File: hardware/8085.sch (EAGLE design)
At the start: 59 parts, among them IC10 74HCT00N, IC11 74HCT245DW, IC2 74HCT574N, IC3 ATF16V8BP3, IC4 74AC00D, IC5 74HCT245DW, IC6 74AC273N, IC7 74HCT139N, IC9 74HCT138N

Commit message: CPU board design updated. 7474 chip added to synchronize address decoders activity with ALE line.
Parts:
- added C12: 100n, rcl:C-EUC0805
- added IC8: 74HCT74N, 74xx-eu:74HCT74N
- added R18: (no value), rcl:R-EU_0204/5
- R17: device rcl:R-EU_0207/10 -> rcl:R-EU_0204/7
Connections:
- new net IO_M_SYNC: IC3.I5, IC8B.Q, IC9A.G1
- new net N$17: IC8A.PRE, IC8B.CLR, IC8B.PRE, R18.1
- net !ALE: now also IC8B.CLK
- net GND: now also C12.2, IC8A.CLK, IC8A.CLR, IC8A.D
- net IO_M: now also IC8B.D; no longer IC3.I5, IC9A.G1
- net VCC: now also C12.1, R18.2
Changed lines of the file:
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@@
 <part name="R15" library="rcl" deviceset="R-EU_" device="0204/7"/>
 <part name="R16" library="rcl" deviceset="R-EU_" device="0204/7"/>
-<part name="R17" library="rcl" deviceset="R-EU_" device="0207/10"/>
+<part name="R17" library="rcl" deviceset="R-EU_" device="0204/7"/>
+<part name="IC8" library="74xx-eu" deviceset="74*74" device="N" technology="HCT"/>
+<part name="GND21" library="supply1" deviceset="GND" device=""/>
+<part name="R18" library="rcl" deviceset="R-EU_" device="0204/5"/>
+<part name="C12" library="rcl" deviceset="C-EU" device="C0805" value="100n"/>
 </parts>
 <sheets>
@@
 <instance part="R16" gate="G$1" x="50.8" y="7.62" rot="R90"/>
 <instance part="R17" gate="G$1" x="73.66" y="-109.22" rot="R90"/>
+<instance part="IC8" gate="A" x="12.7" y="-200.66"/>
+<instance part="IC8" gate="B" x="58.42" y="-200.66"/>
+<instance part="GND21" gate="1" x="-2.54" y="-210.82"/>
+<instance part="R18" gate="G$1" x="-2.54" y="-180.34" rot="R90"/>
+<instance part="C12" gate="G$1" x="236.22" y="137.16"/>
 </instances>
 <busses>
@@
 <wire x1="228.6" y1="142.24" x2="228.6" y2="139.7" width="0.1524" layer="91"/>
 <junction x="220.98" y="142.24"/>
+<pinref part="C12" gate="G$1" pin="1"/>
+<wire x1="228.6" y1="142.24" x2="236.22" y2="142.24" width="0.1524" layer="91"/>
+<wire x1="236.22" y1="142.24" x2="236.22" y2="139.7" width="0.1524" layer="91"/>
+<junction x="228.6" y="142.24"/>
 </segment>
 <segment>
@@
 <wire x1="73.66" y1="-114.3" x2="73.66" y2="-116.84" width="0.1524" layer="91"/>
 <label x="73.66" y="-116.84" size="1.4224" layer="95" rot="R270" xref="yes"/>
+</segment>
+<segment>
+<pinref part="R18" gate="G$1" pin="2"/>
+<wire x1="-2.54" y1="-175.26" x2="-2.54" y2="-172.72" width="0.1524" layer="91"/>
 </segment>
 </net>
@@
 <wire x1="228.6" y1="129.54" x2="228.6" y2="132.08" width="0.1524" layer="91"/>
 <junction x="220.98" y="129.54"/>
+<pinref part="C12" gate="G$1" pin="2"/>
+<wire x1="228.6" y1="129.54" x2="236.22" y2="129.54" width="0.1524" layer="91"/>
+<wire x1="236.22" y1="129.54" x2="236.22" y2="132.08" width="0.1524" layer="91"/>
+<junction x="228.6" y="129.54"/>
 </segment>
 <segment>
@@
 <wire x1="48.26" y1="-147.32" x2="48.26" y2="-154.94" width="0.1524" layer="91"/>
 </segment>
+<segment>
+<pinref part="IC8" gate="A" pin="CLR"/>
+<pinref part="GND21" gate="1" pin="GND"/>
+<wire x1="0" y1="-205.74" x2="-2.54" y2="-205.74" width="0.1524" layer="91"/>
+<wire x1="-2.54" y1="-205.74" x2="-2.54" y2="-208.28" width="0.1524" layer="91"/>
+<pinref part="IC8" gate="A" pin="CLK"/>
+<wire x1="0" y1="-203.2" x2="-2.54" y2="-203.2" width="0.1524" layer="91"/>
+<wire x1="-2.54" y1="-203.2" x2="-2.54" y2="-205.74" width="0.1524" layer="91"/>
+<junction x="-2.54" y="-205.74"/>
+<pinref part="IC8" gate="A" pin="D"/>
+<wire x1="0" y1="-198.12" x2="-2.54" y2="-198.12" width="0.1524" layer="91"/>
+<wire x1="-2.54" y1="-198.12" x2="-2.54" y2="-203.2" width="0.1524" layer="91"/>
+<junction x="-2.54" y="-203.2"/>
+</segment>
 </net>
 <net name="D0" class="0">
@@
 </segment>
 <segment>
-<pinref part="IC3" gate="G$1" pin="I5"/>
-<wire x1="48.26" y1="-93.98" x2="43.18" y2="-93.98" width="0.1524" layer="91"/>
-<label x="43.18" y="-93.98" size="1.4224" layer="95" rot="R180" xref="yes"/>
-</segment>
-<segment>
-<pinref part="IC9" gate="A" pin="G1"/>
-<wire x1="116.84" y1="-144.78" x2="111.76" y2="-144.78" width="0.1524" layer="91"/>
-<label x="111.76" y="-144.78" size="1.4224" layer="95" rot="R180" xref="yes"/>
-</segment>
-<segment>
 <pinref part="SV2" gate="1" pin="39"/>
 <wire x1="160.02" y1="-22.86" x2="165.1" y2="-22.86" width="0.1524" layer="91"/>
 <label x="165.1" y="-22.86" size="1.4224" layer="95" xref="yes"/>
+</segment>
+<segment>
+<pinref part="IC8" gate="B" pin="D"/>
+<wire x1="45.72" y1="-198.12" x2="35.56" y2="-198.12" width="0.1524" layer="91"/>
 </segment>
 </net>
@@
 <label x="-7.62" y="119.38" size="1.4224" layer="95" rot="R180" xref="yes"/>
 </segment>
-</net>
+<segment>
+<pinref part="IC8" gate="B" pin="CLK"/>
+<wire x1="45.72" y1="-203.2" x2="35.56" y2="-203.2" width="0.1524" layer="91"/>
+</segment>
+</net>
+<net name="N$17" class="0">
+<segment>
+<pinref part="IC8" gate="A" pin="PRE"/>
+<pinref part="R18" gate="G$1" pin="1"/>
+<wire x1="0" y1="-195.58" x2="-2.54" y2="-195.58" width="0.1524" layer="91"/>
+<wire x1="-2.54" y1="-195.58" x2="-2.54" y2="-187.96" width="0.1524" layer="91"/>
+<wire x1="-2.54" y1="-187.96" x2="-2.54" y2="-185.42" width="0.1524" layer="91"/>
+<wire x1="-2.54" y1="-187.96" x2="43.18" y2="-187.96" width="0.1524" layer="91"/>
+<wire x1="43.18" y1="-187.96" x2="43.18" y2="-195.58" width="0.1524" layer="91"/>
+<junction x="-2.54" y="-187.96"/>
+<pinref part="IC8" gate="B" pin="PRE"/>
+<wire x1="43.18" y1="-195.58" x2="45.72" y2="-195.58" width="0.1524" layer="91"/>
+<wire x1="43.18" y1="-195.58" x2="43.18" y2="-205.74" width="0.1524" layer="91"/>
+<junction x="43.18" y="-195.58"/>
+<pinref part="IC8" gate="B" pin="CLR"/>
+<wire x1="43.18" y1="-205.74" x2="45.72" y2="-205.74" width="0.1524" layer="91"/>
+</segment>
+</net>
+<net name="IO_M_SYNC" class="0">
+<segment>
+<pinref part="IC8" gate="B" pin="Q"/>
+<wire x1="71.12" y1="-195.58" x2="78.74" y2="-195.58" width="0.1524" layer="91"/>
+</segment>
+<segment>
+<pinref part="IC9" gate="A" pin="G1"/>
+<wire x1="116.84" y1="-144.78" x2="111.76" y2="-144.78" width="0.1524" layer="91"/>
+<label x="111.76" y="-144.78" size="1.4224" layer="95" rot="R180" xref="yes"/>
+</segment>
+<segment>
+<pinref part="IC3" gate="G$1" pin="I5"/>
+<wire x1="48.26" y1="-93.98" x2="43.18" y2="-93.98" width="0.1524" layer="91"/>
+<label x="43.18" y="-93.98" size="1.4224" layer="95" rot="R180" xref="yes"/>
+</segment>
+</net>

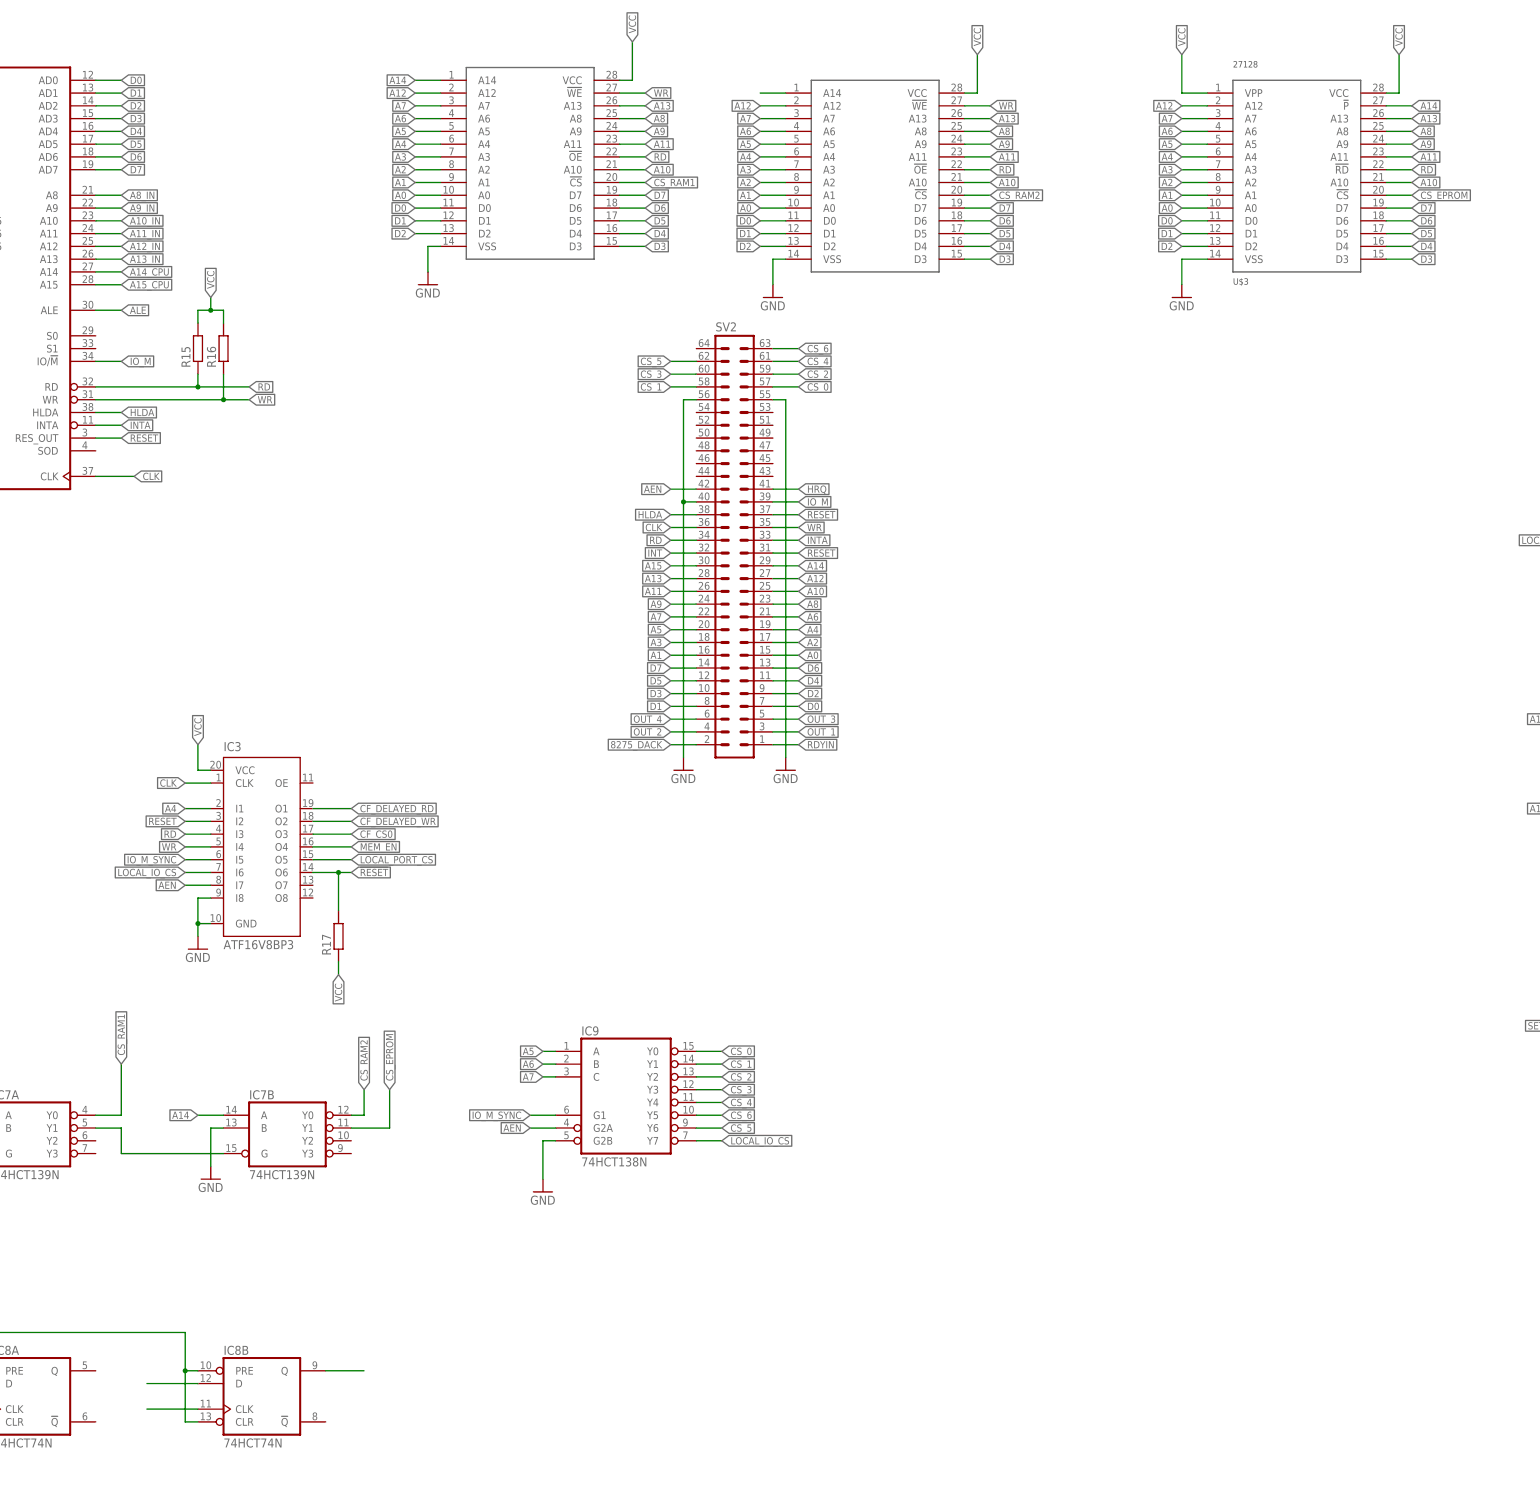
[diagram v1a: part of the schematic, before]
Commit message: Bug in PCB design fixed
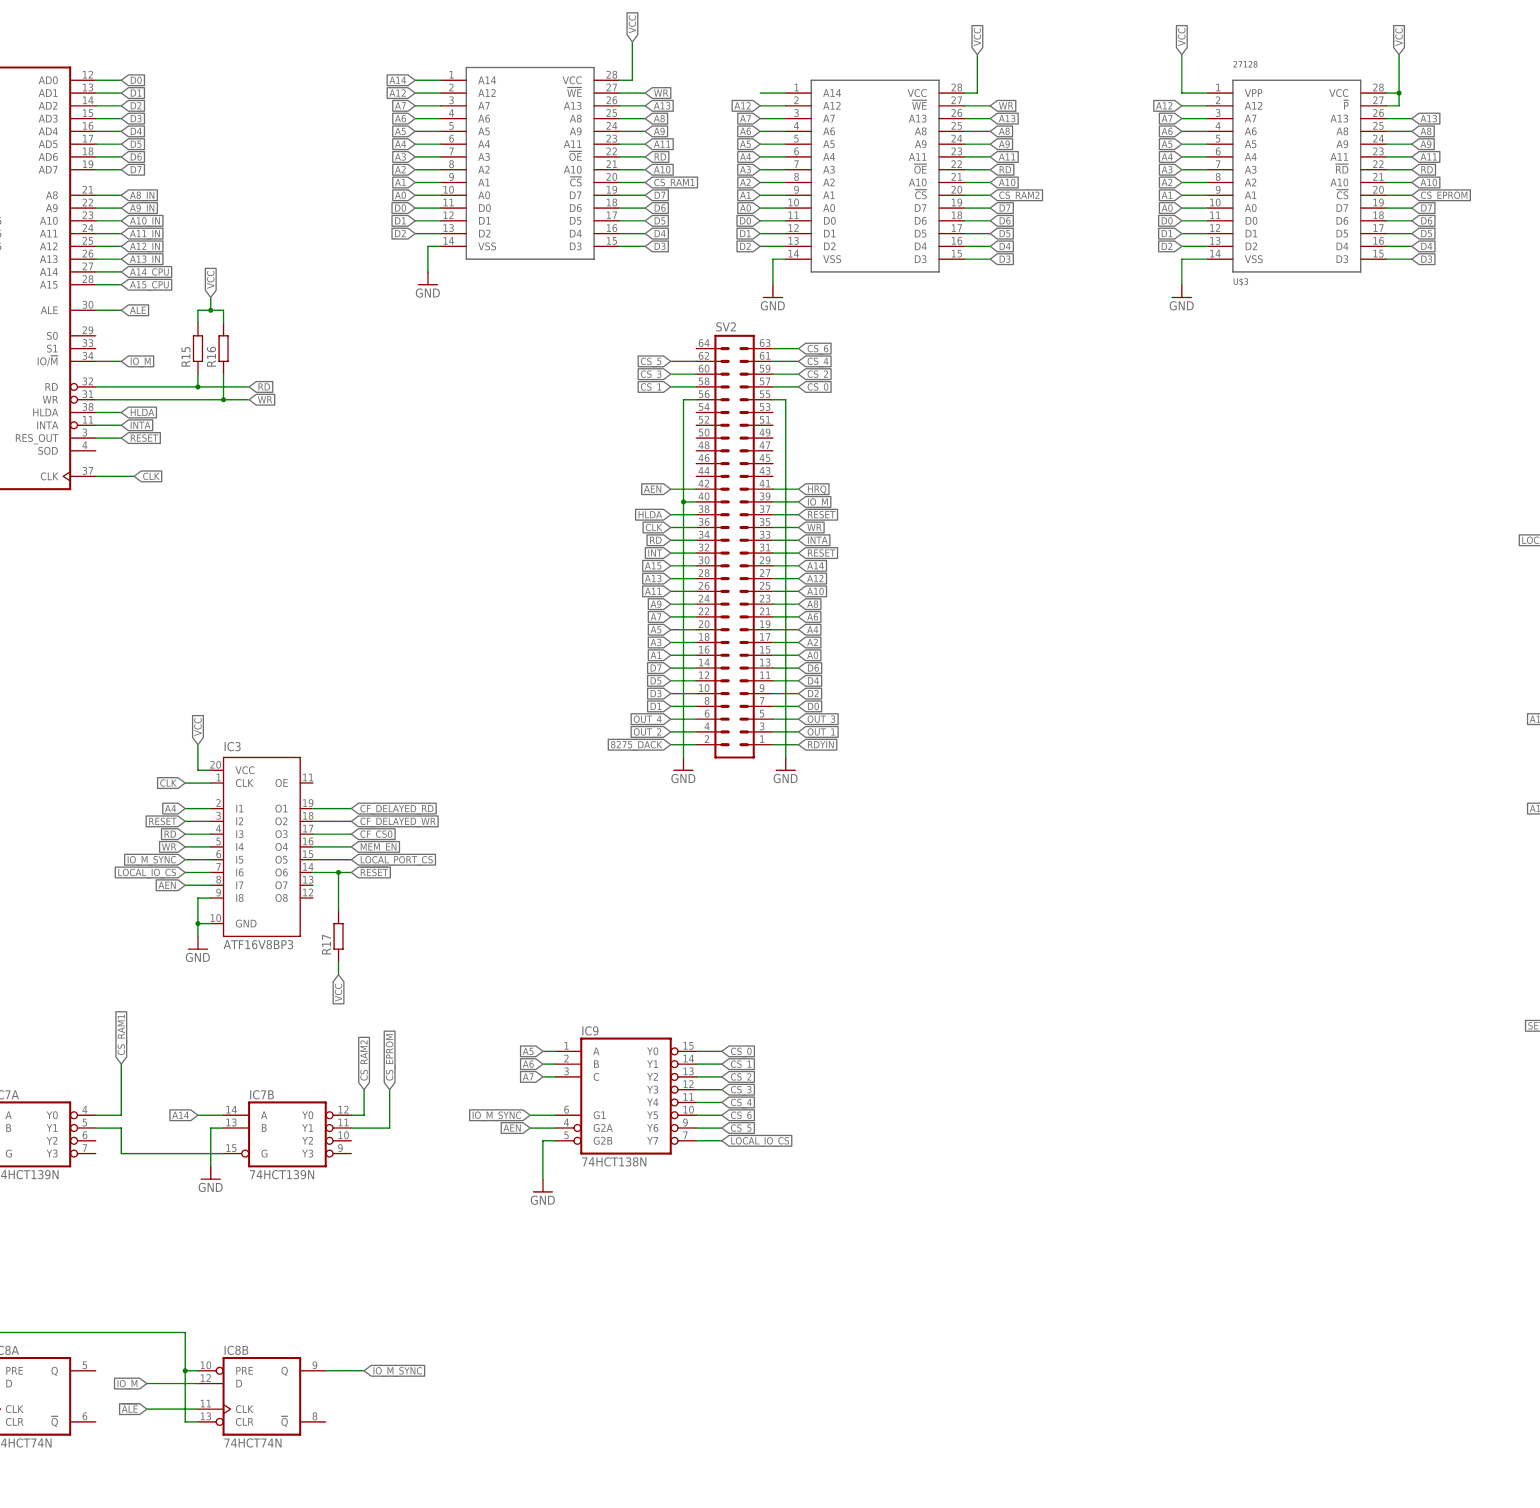
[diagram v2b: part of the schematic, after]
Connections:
- net A14: no longer U$3.!P
- net VCC: now also U$3.!P
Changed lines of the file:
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@@
 <wire x1="284.48" y1="58.42" x2="284.48" y2="66.04" width="0.1524" layer="91"/>
 <label x="284.48" y="66.04" size="1.4224" layer="95" rot="R90" xref="yes"/>
+<pinref part="U$3" gate="G$1" pin="!P"/>
+<wire x1="281.94" y1="55.88" x2="284.48" y2="55.88" width="0.1524" layer="91"/>
+<wire x1="284.48" y1="55.88" x2="284.48" y2="58.42" width="0.1524" layer="91"/>
+<junction x="284.48" y="58.42"/>
 </segment>
 <segment>
@@
 </segment>
 <segment>
-<pinref part="U$3" gate="G$1" pin="!P"/>
-<wire x1="281.94" y1="55.88" x2="287.02" y2="55.88" width="0.1524" layer="91"/>
-<label x="287.02" y="55.88" size="1.4224" layer="95" xref="yes"/>
-</segment>
-<segment>
 <pinref part="IC5" gate="A" pin="A2"/>
 <wire x1="22.86" y1="233.68" x2="27.94" y2="233.68" width="0.1524" layer="91"/>
@@
 <pinref part="IC8" gate="B" pin="D"/>
 <wire x1="45.72" y1="-198.12" x2="35.56" y2="-198.12" width="0.1524" layer="91"/>
+<label x="35.56" y="-198.12" size="1.4224" layer="95" rot="R180" xref="yes"/>
 </segment>
 </net>
@@
 <pinref part="IC8" gate="B" pin="CLK"/>
 <wire x1="45.72" y1="-203.2" x2="35.56" y2="-203.2" width="0.1524" layer="91"/>
+<label x="35.56" y="-203.2" size="1.4224" layer="95" rot="R180" xref="yes"/>
 </segment>
 </net>
@@
 <pinref part="IC8" gate="B" pin="Q"/>
 <wire x1="71.12" y1="-195.58" x2="78.74" y2="-195.58" width="0.1524" layer="91"/>
-</segment>
-<segment>
+<label x="78.74" y="-195.58" size="1.4224" layer="95" xref="yes"/>
+</segment>
+<segment>
